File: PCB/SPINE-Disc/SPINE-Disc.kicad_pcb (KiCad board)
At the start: 2 copper layers, 49 x 49 mm, 29 parts, among them Q1 NTMFS5C628NLT1G, Q2 NTMFS5C628NLT1G, Q3 NTMFS5C628NLT1G, U1 LM311, U3 TL431DBZ

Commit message: update
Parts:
- removed C48: 10uF, Capacitor_SMD:C_1206_3216Metric
- removed D1, D5: LED, LED_SMD:LED_0603_1608Metric
- removed D6: D_Zener, Diode_SMD:D_SOD-323
- removed R2, R6: 1K, Resistor_SMD:R_0603_1608Metric
- removed TP3, TP4, TP5: TestPoint, TestPoint:TestPoint_Pad_D1.0mm
- removed U1: LM311, Package_SO:SOIC-8_3.9x4.9mm_P1.27mm
- added C1: 10uF, Capacitor_SMD:C_1206_3216Metric, F.Cu at (100.5, 87.0)
- added C2: 10uF, Capacitor_SMD:C_1206_3216Metric, F.Cu at (93.5, 87.0)
- added C3: 10uF, Capacitor_SMD:C_1206_3216Metric, F.Cu at (106.0, 97.9)
- added R10: 1M, Resistor_SMD:R_0603_1608Metric, F.Cu at (101.6, 95.5)
- added R11: 100K, Resistor_SMD:R_0603_1608Metric, F.Cu at (101.6, 92.5)
- added R12: 10K, Resistor_SMD:R_0603_1608Metric, F.Cu at (101.6, 94.0)
- added R13: R, Resistor_SMD:R_0603_1608Metric, F.Cu at (95.5, 90.2)
- added R7: 1M, Resistor_SMD:R_0603_1608Metric, F.Cu at (108.1, 106.5)
- added R8: 1M, Resistor_SMD:R_0603_1608Metric, F.Cu at (102.2, 106.5)
- added R9: 1M, Resistor_SMD:R_0603_1608Metric, F.Cu at (113.9, 106.5)
- added U2: MX5709T, Package_TO_SOT_SMD:TSOT-23-5, F.Cu at (97.0, 87.0)
- added U4: LM393, Package_SO:SOIC-8_3.9x4.9mm_P1.27mm, F.Cu at (107.0, 94.0)
- R1: value 1K -> 100K
- R3: value 1M -> 4.7K
- R4: value 1M -> R
- moved D4 66.4 mm to (83.3, 123.0), turned to 90 degrees
- moved R1 56.4 mm to (84.8, 123.0), turned to -90 degrees
- moved D3 51.8 mm to (91.0, 100.0), turned to -90 degrees
- moved R3 42.1 mm to (102.7, 86.4), turned to 90 degrees
- moved U3 40.9 mm to (105.4, 87.9)
- moved C21 37.9 mm to (102.7, 89.4), turned to -90 degrees
- moved R4 37.5 mm to (98.5, 90.2), turned to 180 degrees
- moved R5 33.7 mm to (108.1, 103.1), turned to -90 degrees
- moved Q3 0.11 mm to (104.1, 111.6)
- moved Q1 0.10 mm to (115.8, 111.6)
- moved Q2 0.10 mm to (110.0, 111.6)
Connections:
- Q1 pad 4: BRAKE_GATE -> Net-(Q1-G)
- Q2 pad 4: BRAKE_GATE -> Net-(Q2-G)
- Q3 pad 4: BRAKE_GATE -> Net-(Q3-G)
- R4 pad 2: VDC -> Net-(U2-SENSE/ADJ)
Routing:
- net +12V: track 0.00 -> 37.3 mm
- net VDC: track 0.00 -> 29.5 mm
- net BRAKE_GATE: track 0.00 -> 27.6 mm
- net +2V5: track 0.00 -> 12.4 mm
- net Net-(U4B-+): track 0.00 -> 5.89 mm
- net Net-(U2-SENSE/ADJ): track 0.00 -> 3.79 mm
- net Net-(D4-A): track 0.00 -> 2.23 mm
- net Net-(Q1-G): track 0.00 -> 1.55 mm
- net Net-(Q3-G): track 0.00 -> 1.55 mm
- net Net-(Q2-G): track 0.00 -> 1.55 mm
- net GND: track 0.00 -> 0.64 mm, vias 0 -> 175
- added copper zone on F.Cu, net GND
- added copper zone on F.Cu, net PRI_HI
- added copper zone on B.Cu, net RESISTOR-
- added copper zone on F.Cu, net RESISTOR-
- added copper zone on B.Cu, net unconnected-(H1-Pad1)
- added copper zone on F.Cu, net unconnected-(H1-Pad1)
- added copper zone on B.Cu, net unconnected-(H2-Pad1)
- added copper zone on F.Cu, net unconnected-(H2-Pad1)
- added copper zone on B.Cu, net unconnected-(H3-Pad1)
- added copper zone on F.Cu, net unconnected-(H3-Pad1)
- added copper zone on B.Cu, net unconnected-(H4-Pad1)
- added copper zone on F.Cu, net unconnected-(H4-Pad1)

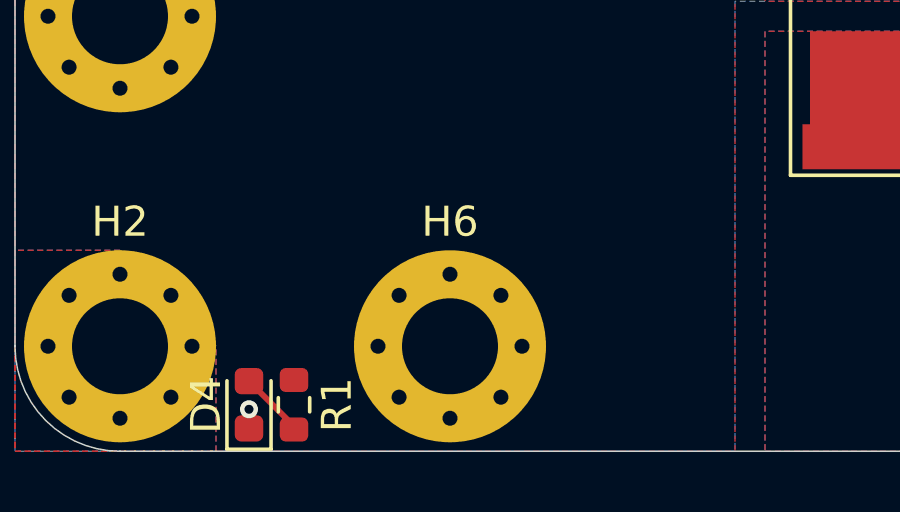
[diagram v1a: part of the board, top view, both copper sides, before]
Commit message: Vertebra fix
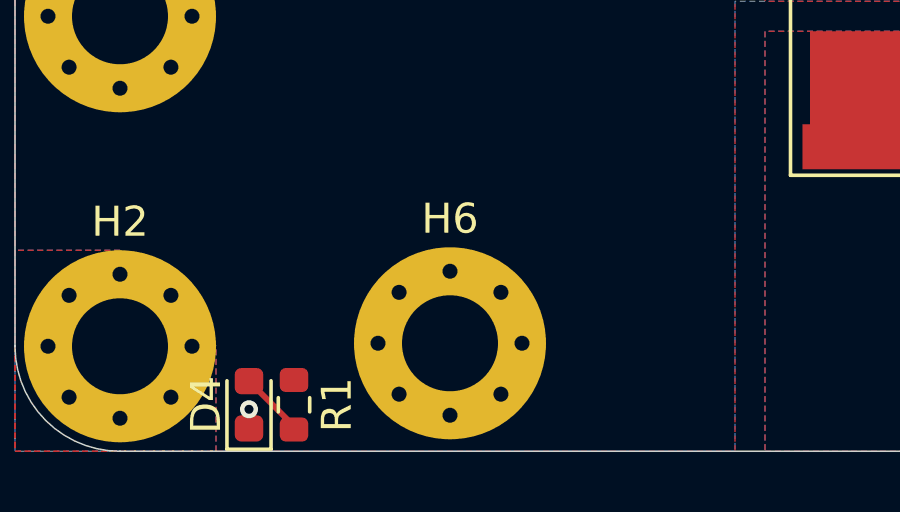
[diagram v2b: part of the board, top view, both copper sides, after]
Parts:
- added G***: LOGO, LOGO, F.Cu at (90.5, 110.0)
- moved H6 0.10 mm to (90.0, 120.9)

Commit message: update
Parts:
- C1: value 10uF -> 100nF; footprint Capacitor_SMD:C_1206_3216Metric -> Capacitor_SMD:C_0805_2012Metric
- R7, R8, R9: value 1M -> 10R
- moved C3 12.2 mm to (100.5, 87.0), turned to 90 degrees
- moved C1 12.1 mm to (105.5, 98.0), turned to 180 degrees
- moved R12 3.47 mm to (99.0, 96.3), turned to -90 degrees
- moved R11 2.72 mm to (99.0, 93.3), turned to -90 degrees
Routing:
- net Net-(U4B-+): track 5.89 -> 9.02 mm
- net VDC: track 29.5 -> 27.7 mm
- net GND: vias 175 -> 176

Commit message: update
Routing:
- net VDC: track 27.7 -> 28.9 mm
- net Net-(U4B-+): track 9.02 -> 9.80 mm
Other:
- board text added: "+"

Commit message: update
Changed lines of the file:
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@@
+	)
+	(gr_line
+		(start 100.5 123)
+		(end 102.5 119)
+		(stroke
+			(width 0.8)
+			(type solid)
+		)
+		(layer "F.SilkS")
+	)
+	(gr_line
+		(start 95 121)
+		(end 97 121)
+		(stroke
+			(width 0.8)
+			(type solid)
+		)
+		(layer "F.SilkS")
+	)
+	(gr_line
+		(start 103 121)
+		(end 105 121)
+		(stroke
+			(width 0.8)
+			(type solid)
+		)
+		(layer "F.SilkS")
+	)
+	(gr_line
+		(start 99 123)
+		(end 101 119)
+		(stroke
+			(width 0.8)
+			(type solid)
+		)
+		(layer "F.SilkS")
+	)
+	(gr_line
+		(start 97.5 123)
+		(end 99.5 119)
+		(stroke
+			(width 0.8)
+			(type solid)
+		)
+		(layer "F.SilkS")
+	)
+	(gr_line
+		(start 97 121)
+		(end 98 119)
+		(stroke
+			(width 0.8)
+			(type solid)
+		)
+		(layer "F.SilkS")
+	)
+	(gr_line
+		(start 102 123)
+		(end 103 121)
+		(stroke
+			(width 0.8)
+			(type solid)
+		)
+		(layer "F.SilkS")
 	)
 	(gr_line
